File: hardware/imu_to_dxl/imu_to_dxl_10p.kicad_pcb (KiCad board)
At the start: 2 copper layers, 141.9 x 72.9 mm, 862 parts, among them CN1 B3B-EH-A (LF)(SN), CN2 B3B-PH-K-S(LF)(SN), J1 1.8mm螺丝孔, J2 1.8mm螺丝孔, J3 1.8mm螺丝孔, J4 1.8mm螺丝孔, Q1 MMBT3906, U1 ETA2845S2G_C22362741, U2 GD32F303CCT6, U3 LSM6DSV16XTR, U4 SN74LVC1G126DBVR, U5 SN74LVC1G125DBV, U6 ME6211C18M5G-N, X1 XL2EL89CSI-111YLC-12M

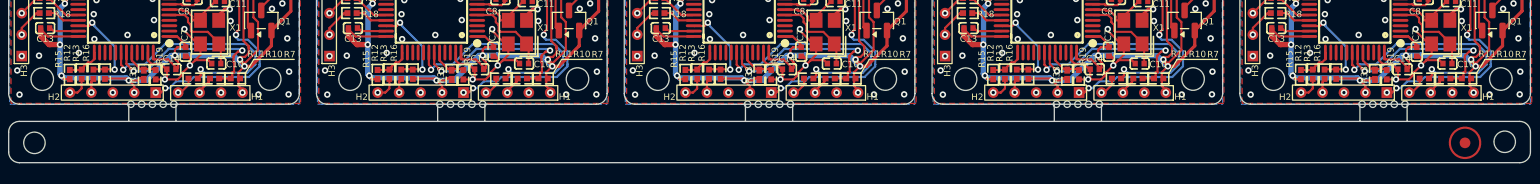
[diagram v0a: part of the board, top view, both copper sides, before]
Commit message: 更新原理和PCB，优化飞特舵机上拉电阻小导致小概率丢包问题
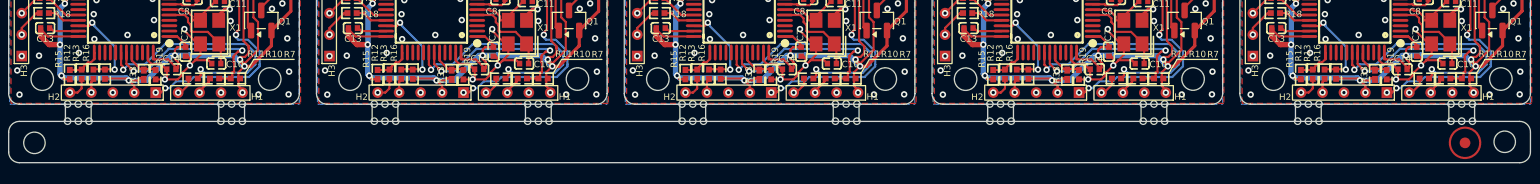
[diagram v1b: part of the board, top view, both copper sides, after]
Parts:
- removed the REF** at (178.8, 165.4)
- removed the REF** at (64.0, 165.4)
- removed the REF** at (180.8, 165.4)
- removed the REF** at (124.5, 165.4)
- removed the REF** at (68.0, 165.4)
- removed the REF** at (94.8, 165.4)
- removed the REF** at (152.3, 165.4)
- removed the REF** at (151.3, 165.4)
- removed the REF** at (125.5, 165.4)
- removed the REF** at (93.8, 165.4)
- removed the REF** at (67.0, 165.4)
- removed the REF** at (122.5, 165.4)
- removed the REF** at (179.8, 165.4)
- removed the REF** at (150.3, 165.4)
- removed the REF** at (66.0, 165.4)
- removed the REF** at (65.0, 165.4)
- removed the REF** at (123.5, 165.4)
- removed the REF** at (182.8, 165.4)
- removed the REF** at (154.3, 165.4)
- removed the REF** at (181.8, 165.4)
- removed the REF** at (153.3, 165.4)
- removed the REF** at (121.5, 165.4)
- removed the REF** at (92.8, 165.4)
- removed the REF** at (96.8, 165.4)
- removed the REF** at (95.8, 165.4)
- added REF**: mailslot, microduck:mailslot, F.Cu at (72.4, 167.0)
- added REF**: mailslot, microduck:mailslot, F.Cu at (101.0, 167.0)
- added REF**: mailslot, microduck:mailslot, F.Cu at (87.7, 167.0)
- added REF**: mailslot, microduck:mailslot, F.Cu at (115.4, 167.0)
- added REF**: mailslot, microduck:mailslot, F.Cu at (117.4, 165.4)
- added REF**: mailslot, microduck:mailslot, F.Cu at (73.4, 165.4)
- added REF**: mailslot, microduck:mailslot, F.Cu at (103.0, 165.4)
- added REF**: mailslot, microduck:mailslot, F.Cu at (60.1, 165.4)
- added REF**: mailslot, microduck:mailslot, F.Cu at (145.1, 165.4)
- added REF**: mailslot, microduck:mailslot, F.Cu at (73.4, 167.0)
- added REF**: mailslot, microduck:mailslot, F.Cu at (159.4, 167.0)
- added REF**: mailslot, microduck:mailslot, F.Cu at (86.7, 167.0)
- added REF**: mailslot, microduck:mailslot, F.Cu at (116.4, 165.4)
- added REF**: mailslot, microduck:mailslot, F.Cu at (172.8, 167.0)
- added REF**: mailslot, microduck:mailslot, F.Cu at (60.1, 167.0)
- added REF**: mailslot, microduck:mailslot, F.Cu at (173.8, 165.4)
- added REF**: mailslot, microduck:mailslot, F.Cu at (146.1, 167.0)
- added REF**: mailslot, microduck:mailslot, F.Cu at (88.7, 167.0)
- added REF**: mailslot, microduck:mailslot, F.Cu at (188.1, 167.0)
- added REF**: mailslot, microduck:mailslot, F.Cu at (174.8, 167.0)
- added REF**: mailslot, microduck:mailslot, F.Cu at (87.7, 165.4)
- added REF**: mailslot, microduck:mailslot, F.Cu at (159.4, 165.4)
- added REF**: mailslot, microduck:mailslot, F.Cu at (160.4, 165.4)
- added REF**: mailslot, microduck:mailslot, F.Cu at (131.7, 165.4)
- added REF**: mailslot, microduck:mailslot, F.Cu at (158.4, 167.0)
- added REF**: mailslot, microduck:mailslot, F.Cu at (103.0, 167.0)
- added REF**: mailslot, microduck:mailslot, F.Cu at (102.0, 167.0)
- added REF**: mailslot, microduck:mailslot, F.Cu at (74.4, 167.0)
- added REF**: mailslot, microduck:mailslot, F.Cu at (130.7, 165.4)
- added REF**: mailslot, microduck:mailslot, F.Cu at (102.0, 165.4)
- added REF**: mailslot, microduck:mailslot, F.Cu at (144.1, 167.0)
- added REF**: mailslot, microduck:mailslot, F.Cu at (173.8, 167.0)
- added REF**: mailslot, microduck:mailslot, F.Cu at (174.8, 165.4)
- added REF**: mailslot, microduck:mailslot, F.Cu at (88.7, 165.4)
- added REF**: mailslot, microduck:mailslot, F.Cu at (158.4, 165.4)
- added REF**: mailslot, microduck:mailslot, F.Cu at (130.7, 167.0)
- added REF**: mailslot, microduck:mailslot, F.Cu at (59.1, 167.0)
- added REF**: mailslot, microduck:mailslot, F.Cu at (72.4, 165.4)
- added REF**: mailslot, microduck:mailslot, F.Cu at (145.1, 167.0)
- added REF**: mailslot, microduck:mailslot, F.Cu at (189.1, 165.4)
- added REF**: mailslot, microduck:mailslot, F.Cu at (117.4, 167.0)
- added REF**: mailslot, microduck:mailslot, F.Cu at (131.7, 167.0)
- added REF**: mailslot, microduck:mailslot, F.Cu at (172.8, 165.4)
- added REF**: mailslot, microduck:mailslot, F.Cu at (144.1, 165.4)
- added REF**: mailslot, microduck:mailslot, F.Cu at (160.4, 167.0)
- added REF**: mailslot, microduck:mailslot, F.Cu at (58.1, 167.0)
- added REF**: mailslot, microduck:mailslot, F.Cu at (86.7, 165.4)
- added REF**: mailslot, microduck:mailslot, F.Cu at (116.4, 167.0)
- added REF**: mailslot, microduck:mailslot, F.Cu at (74.4, 165.4)
- added REF**: mailslot, microduck:mailslot, F.Cu at (188.1, 165.4)
- added REF**: mailslot, microduck:mailslot, F.Cu at (59.1, 165.4)
- added REF**: mailslot, microduck:mailslot, F.Cu at (146.1, 165.4)
- added REF**: mailslot, microduck:mailslot, F.Cu at (58.1, 165.4)
- added REF**: mailslot, microduck:mailslot, F.Cu at (129.7, 165.4)
- added REF**: mailslot, microduck:mailslot, F.Cu at (187.1, 165.4)
- added REF**: mailslot, microduck:mailslot, F.Cu at (101.0, 165.4)
- added REF**: mailslot, microduck:mailslot, F.Cu at (187.1, 167.0)
- added REF**: mailslot, microduck:mailslot, F.Cu at (129.7, 167.0)
- added REF**: mailslot, microduck:mailslot, F.Cu at (115.4, 165.4)
- added REF**: mailslot, microduck:mailslot, F.Cu at (189.1, 167.0)
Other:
- outline, holes or cut-outs redrawn
